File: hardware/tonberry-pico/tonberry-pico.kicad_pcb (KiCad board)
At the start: 2 copper layers, 98 x 53.5 mm, 30 parts, among them J1 MicroSD_Breakout, J2 SparkFun I2S Audio Breakout M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, J3 RC522_Breakout, J4 Adafruit_bq25185_5V, J5 UART, J6 WS2812, J7 Buttons, Q1 2N7000, Q2 2N7000, SW5 SW_Push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

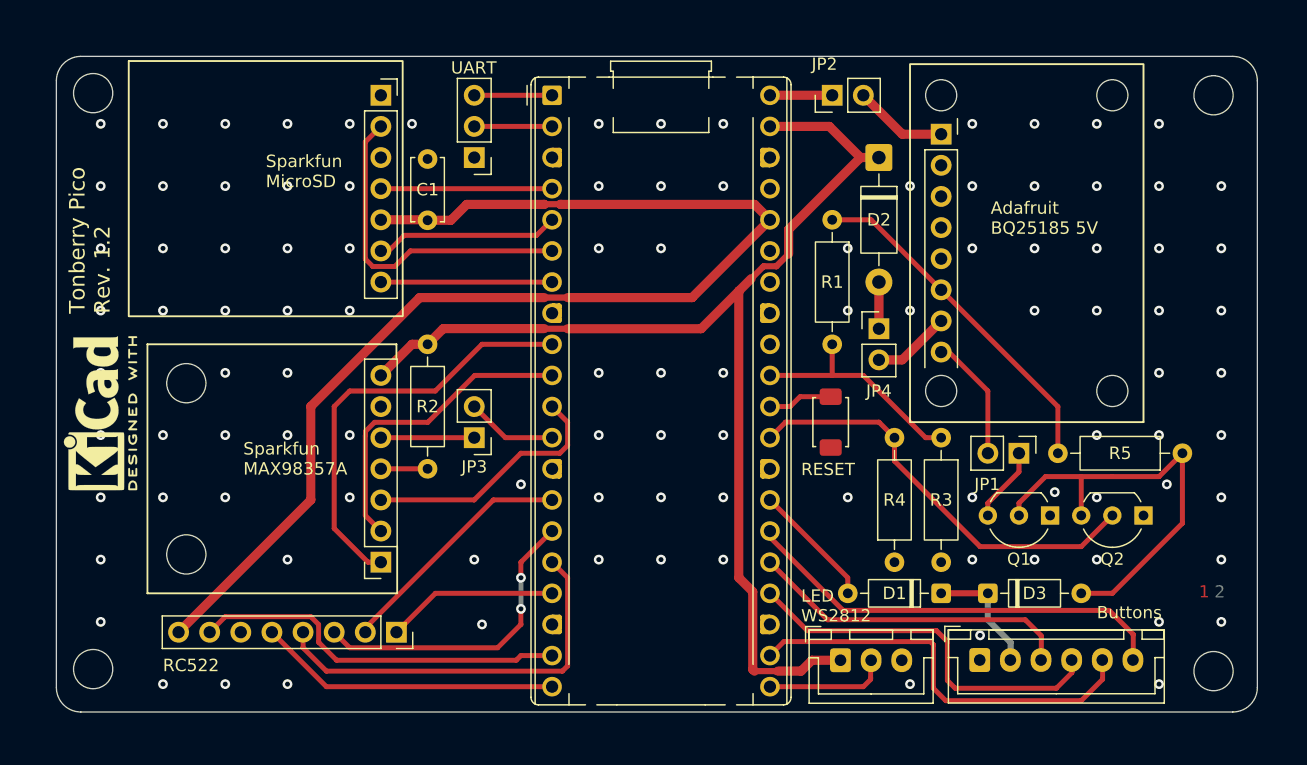
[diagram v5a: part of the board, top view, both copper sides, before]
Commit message: hw: Add GND point for MAX98357 gain config
Add a through-hole pad connected to GND next to the MAX98357 gain config
resistor to allow the user to select from all possible gains.

Signed-off-by: Matthias Blankertz <matthias@blankertz.org>
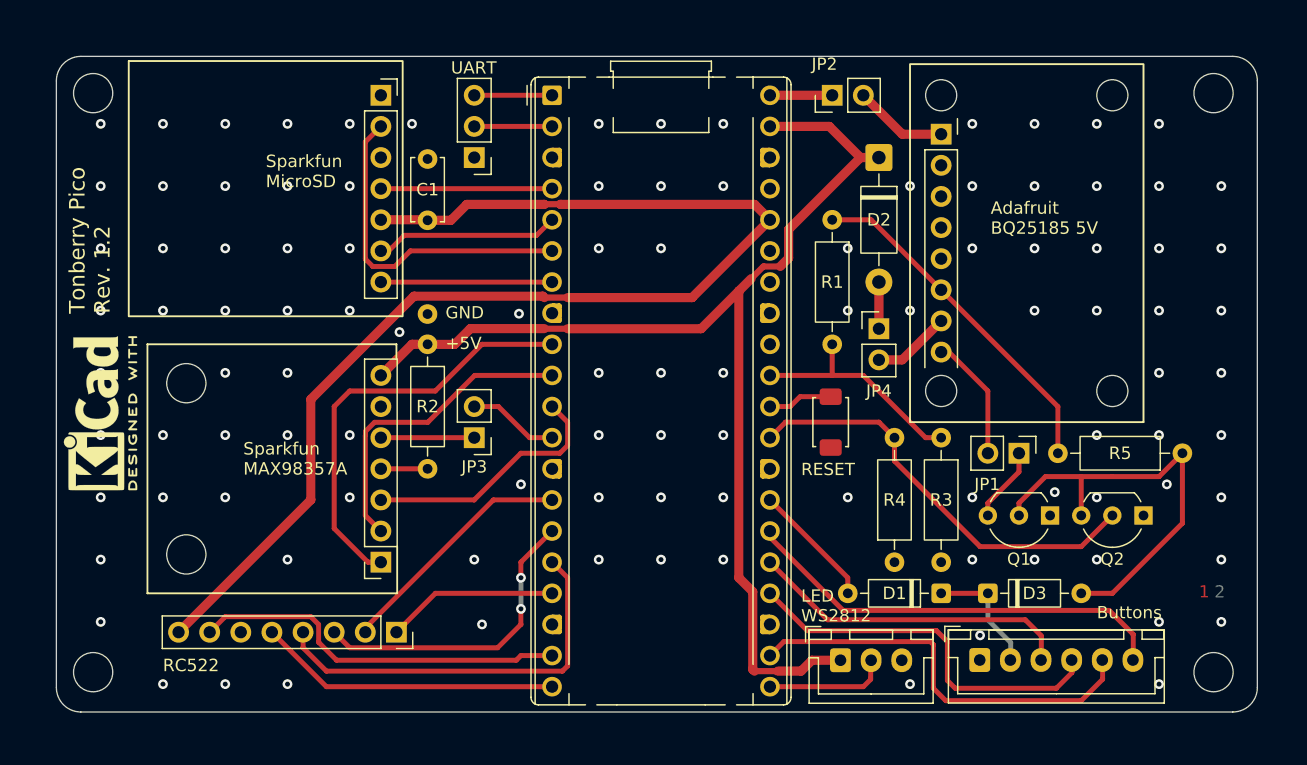
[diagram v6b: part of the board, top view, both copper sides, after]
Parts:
- added J8: Conn_01x01, Connector_Wire:SolderWire-0.25sqmm_1x01_D0.65mm_OD1.7mm, F.Cu at (148.6, 59.1)
- moved REF** 0.25 mm to (121.3, 88.3)
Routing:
- net GND: vias 104 -> 106
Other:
- board text added: "+5V"
- board text added: "GND"
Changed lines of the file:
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@@
 		)
 	)
+	(footprint "Connector_Wire:SolderWire-0.25sqmm_1x01_D0.65mm_OD1.7mm"
+		(layer "F.Cu")
+		(at 148.587019 59.12637)
+		(descr "Soldered wire connection, for a single 0.25 mm² wire, basic insulation, conductor diameter 0.65mm, outer diameter 1.7mm, size source Multi-Contact FLEXI-E_0.25 (https://www.staubli.com/content/dam/ecs/catalogs-brochures/TM/CAB-Main-11014119-en.pdf#page=9), bend radius 3 times outer diameter, generated with kicad-footprint-generator")
+		(tags "connector wire 0.25sqmm")
+		(property "Reference" "J8"
+			(at 0 -2.12 0)
+			(layer "F.SilkS")
+			(hide yes)
+			(effects
+				(font
+					(size 1 1)
+					(thickness 0.15)
+				)
+			)
+		)
+		(property "Value" "Conn_01x01"
+			(at 0 2.12 0)
+			(layer "F.Fab")
+			(effects
+				(font
+					(size 1 1)
+					(thickness 0.15)
+				)
+			)
+		)
+		(property "Datasheet" "~"
+			(at 0 0 0)
+			(layer "F.Fab")
+			(hide yes)
+			(effects
+				(font
+					(size 1.27 1.27)
+					(thickness 0.15)
+				)
+			)
+		)
+		(property "Description" "Generic connector, single row, 01x01, script generated (kicad-library-utils/schlib/autogen/connector/)"
+			(at 0 0 0)
+			(layer "F.Fab")
+			(hide yes)
+			(effects
+				(font
+					(size 1.27 1.27)
+					(thickness 0.15)
+				)
+			)
+		)
+		(property ki_fp_filters "Connector*:*_1x??_*")
+		(sheetname "/")
+		(sheetfile "tonberry-pico.kicad_sch")
+		(attr exclude_from_pos_files)
+		(fp_line
+			(start -1.6 -1.42)
+			(end -1.6 1.42)
+			(stroke
+				(width 0.05)
+				(type solid)
+			)
+			(layer "F.CrtYd")
+		)
+		(fp_line
+			(start -1.6 1.42)
+			(end 1.6 1.42)
+			(stroke
+				(width 0.05)
+				(type solid)
+			)
+			(layer "F.CrtYd")
+		)
+		(fp_line
+			(start 1.6 -1.42)
+			(end -1.6 -1.42)
+			(stroke
+				(width 0.05)
+				(type solid)
+			)
+			(layer "F.CrtYd")
+		)
+		(fp_line
+			(start 1.6 1.42)
+			(end 1.6 -1.42)
+			(stroke
+				(width 0.05)
+				(type solid)
+			)
+			(layer "F.CrtYd")
+		)
+		(fp_circle
+			(center 0 0)
+			(end 0.85 0)
+			(stroke
+				(width 0.1)
+				(type solid)
+			)
+			(fill no)
+			(layer "F.Fab")
+		)
+		(fp_text user "${REFERENCE}"
+			(at 0 0 0)
+			(layer "F.Fab")
+			(effects
+				(font
+					(size 0.42 0.42)
+					(thickness 0.06)
+				)
+			)
+		)
+		(pad "1" thru_hole circle
+			(at 0 0)
+			(size 1.6 1.6)
+			(drill 0.8)
+			(layers "*.Cu" "*.Mask")
+			(remove_unused_layers no)
+			(net 2 "GND")
+			(pinfunction "Pin_1")
+			(pintype "passive")
+		)
+		(embedded_fonts no)
+		(model "${KICAD9_3DMODEL_DIR}/Connector_Wire.3dshapes/SolderWire-0.25sqmm_1x01_D0.65mm_OD1.7mm.step"
+			(offset
+				(xyz 0 0 0)
+			)
+			(scale
+				(xyz 1 1 1)
+			)
+			(rotate
+				(xyz 0 0 0)
+			)
+		)
+	)
 	(footprint "MountingHole:MountingHole_3.2mm_M3_DIN965"
 		(layer "F.Cu")
@@
 		)
 		(pad "" np_thru_hole circle
-			(at 0 0)
+			(at 0 -0.175)
 			(size 3.2 3.2)
 			(drill 3.2)
@@
 		)
 		(pad "" np_thru_hole circle
-			(at 0 0)
+			(at 0 0.085)
 			(size 3.2 3.2)
 			(drill 3.2)
@@
 	(footprint "MountingHole:MountingHole_3.2mm_M3_DIN965"
 		(layer "F.Cu")
-		(at 121.3 88.1)
+		(at 121.3 88.35)
 		(descr "Mounting Hole 3.2mm, M3, no annular, generated by kicad-footprint-generator mountinghole.py")
 		(tags "mountinghole M3 DIN965")
@@
 		(layer "Edge.Cuts")
 	)
+	(gr_text "+5V"
+		(at 150.05 62.1 0)
+		(layer "F.SilkS")
+		(effects
+			(font
+				(size 1 1)
+				(thickness 0.15)
+			)
+			(justify left bottom)
+		)
+	)
 	(gr_text "Sparkfun\nMicroSD"
 		(at 135.382 48.895 0)
@@
 		)
 	)
+	(gr_text "GND"
+		(at 150.05 59.6 0)
+		(layer "F.SilkS")
+		(effects
+			(font
+				(size 1 1)
+				(thickness 0.15)
+			)
+			(justify left bottom)
+		)
+	)
 	(gr_text "LED\nWS2812"
 		(at 179.07 84.328 0)
@@
 	)
 	(segment
+		(start 148.59 61.595)
+		(end 148.595 61.6)
+		(width 0.75)
+		(layer "F.Cu")
+		(net 1)
+	)
+	(segment
 		(start 173.99 80.645)
 		(end 173.99 57.250161)
@@
 	)
 	(segment
-		(start 183.9175 46.355)
-		(end 178.05242 52.22008)
-		(width 0.75)
+		(start 175.99626 55.243902)
+		(end 177.375903 55.243902)
+		(width 0.508)
 		(layer "F.Cu")
 		(net 1)
@@
 	)
 	(segment
-		(start 177.04984 55.23)
-		(end 178.05242 54.22742)
-		(width 0.508)
+		(start 152.085 60.315)
+		(end 158.105002 60.315)
+		(width 0.75)
 		(layer "F.Cu")
 		(net 1)
 	)
 	(segment
-		(start 149.87 60.315)
-		(end 158.105002 60.315)
+		(start 178.05242 54.567385)
+		(end 177.375903 55.243902)
 		(width 0.75)
 		(layer "F.Cu")
@@
 	)
 	(segment
-		(start 176.010162 55.23)
-		(end 177.04984 55.23)
-		(width 0.508)
+		(start 170.915161 60.325)
+		(end 173.99 57.250161)
+		(width 0.75)
 		(layer "F.Cu")
 		(net 1)
 	)
 	(segment
-		(start 170.915161 60.325)
-		(end 173.99 57.250161)
+		(start 148.595 61.6)
+		(end 150.8 61.6)
+		(width 0.75)
+		(layer "F.Cu")
+		(net 1)
+	)
+	(segment
+		(start 178.05242 52.22008)
+		(end 178.05242 54.567385)
 		(width 0.75)
 		(layer "F.Cu")
@@
 	)
 	(segment
-		(start 148.59 61.595)
-		(end 149.87 60.315)
-		(width 0.75)
-		(layer "F.Cu")
-		(net 1)
-	)
-	(segment
 		(start 174.992581 56.247581)
 		(end 173.99 57.250161)
@@
 	)
 	(segment
-		(start 178.05242 52.22008)
-		(end 178.05242 54.22742)
-		(width 0.75)
+		(start 174.992581 56.247581)
+		(end 175.99626 55.243902)
+		(width 0.508)
 		(layer "F.Cu")
 		(net 1)
@@
 	)
 	(segment
-		(start 174.992581 56.247581)
-		(end 176.010162 55.23)
+		(start 160.02 60.325)
+		(end 158.115002 60.325)
 		(width 0.508)
 		(layer "F.Cu")
@@
 	)
 	(segment
-		(start 160.02 60.325)
-		(end 158.115002 60.325)
-		(width 0.508)
+		(start 183.9175 46.355)
+		(end 178.05242 52.22008)
+		(width 0.75)
+		(layer "F.Cu")
+		(net 1)
+	)
+	(segment
+		(start 150.8 61.6)
+		(end 152.085 60.315)
+		(width 0.75)
 		(layer "F.Cu")
 		(net 1)
@@
 	)
 	(via
+		(at 146.3 60.6)
+		(size 0.8)
+		(drill 0.4)
+		(layers "F.Cu" "B.Cu")
+		(free yes)
+		(net 2)
+	)
+	(via
 		(at 172.72 74.085)
 		(size 0.8)
@@
 	)
 	(via
+		(at 156.05 59.1)
+		(size 0.8)
+		(drill 0.4)
+		(layers "F.Cu" "B.Cu")
+		(free yes)
+		(net 2)
+	)
+	(via
 		(at 182.88 74.085)
 		(size 0.8)
@@
 		(start 190.5 81.915)
 		(end 194.31 81.915)
-		(width 0.508)
+		(width 0.4064)
 		(layer "F.Cu")
 		(net 5)
@@
 		(start 196.175 85.939)
 		(end 194.31 84.074)
-		(width 0.508)
+		(width 0.4064)
 		(layer "B.Cu")
 		(net 5)
@@
 		(start 194.31 84.074)
 		(end 194.31 81.915)
-		(width 0.508)
+		(width 0.4064)
 		(layer "B.Cu")
 		(net 5)
@@
 		(start 196.175 86.995)
 		(end 196.175 85.939)
-		(width 0.508)
+		(width 0.4064)
 		(layer "B.Cu")
 		(net 5)
@@
 	)
 	(segment
-		(start 150.495 51.475)
-		(end 151.79 50.18)
+		(start 157.997452 57.66745)
+		(end 158.115002 57.785)
 		(width 0.75)
 		(layer "F.Cu")
@@
 	)
 	(segment
-		(start 139.065 74.295)
-		(end 139.065 66.665)
+		(start 150.495 51.475)
+		(end 151.79 50.18)
 		(width 0.75)
 		(layer "F.Cu")
@@
 	)
 	(segment
-		(start 139.065 66.665)
-		(end 147.945 57.785)
-		(width 0.75)
-		(layer "F.Cu")
-		(net 13)
-	)
-	(segment
 		(start 150.495 51.475)
 		(end 148.59 51.475)
@@
 	)
 	(segment
+		(start 139.065 66.085)
+		(end 147.48255 57.66745)
+		(width 0.75)
+		(layer "F.Cu")
+		(net 13)
+	)
+	(segment
 		(start 158.1 50.18)
 		(end 158.115 50.165)
@@
 	)
 	(segment
-		(start 170.195 57.77)
-		(end 176.53 51.435)
+		(start 139.065 74.295)
+		(end 139.065 66.085)
 		(width 0.75)
 		(layer "F.Cu")
@@
 	)
 	(segment
-		(start 147.945 57.785)
-		(end 158.115002 57.785)
+		(start 170.195 57.77)
+		(end 176.53 51.435)
 		(width 0.75)
 		(layer "F.Cu")
@@
 	)
 	(segment
+		(start 147.48255 57.66745)
+		(end 157.997452 57.66745)
+		(width 0.75)
+		(layer "F.Cu")
+		(net 13)
+	)
+	(segment
 		(start 158.115 50.165)
 		(end 159.425958 50.165)
@@
 	)
 	(segment
+		(start 158.709565 69.174565)
+		(end 158.75 69.215)
+		(width 0.2032)
+		(layer "F.Cu")
+		(net 47)
+	)
+	(segment
 		(start 152.4 66.675)
-		(end 154.94 69.215)
+		(end 154.375 66.675)
 		(width 0.4064)
 		(layer "F.Cu")
@@
 	)
 	(segment
-		(start 158.709565 69.174565)
+		(start 156.915 69.215)
 		(end 158.75 69.215)
-		(width 0.2032)
+		(width 0.4064)
 		(layer "F.Cu")
 		(net 47)
 	)
 	(segment
-		(start 154.94 69.215)
-		(end 158.75 69.215)
+		(start 154.375 66.675)
+		(end 156.915 69.215)
 		(width 0.4064)
 		(layer "F.Cu")

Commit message: hw: Update metadata, move silkscreen board name + rev
No netlist or routing changes.

Signed-off-by: Matthias Blankertz <matthias@blankertz.org>
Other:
- board text added: "Tonberry Pico Rev. ${REVISION} ${ISSUE_DATE}"
- board text removed: "Tonberry Pico Rev. 1.2"
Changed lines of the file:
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@@
 	)
 	(paper "A4")
+	(title_block
+		(title "Tonberry Pico")
+		(date "2025-11-08")
+		(rev "1.2")
+		(comment 1 "Copyright (c) 2025 Matthias Blankertz <matthias@blankertz.org>")
+		(comment 2 "SPDX-License-Identifier: MIT")
+	)
 	(layers
 		(0 "F.Cu" signal)
@@
 	)
 	(footprint "MountingHole:MountingHole_3.2mm_M3_DIN965"
+		(locked yes)
 		(layer "F.Cu")
 		(at 212.725 41.275)
@@
 	)
 	(footprint "MountingHole:MountingHole_3.2mm_M3_DIN965"
+		(locked yes)
 		(layer "F.Cu")
 		(at 212.725 88.265)
@@
 	)
 	(footprint "MountingHole:MountingHole_3.2mm_M3_DIN965"
+		(locked yes)
 		(layer "F.Cu")
 		(at 121.3 41.1)
@@
 	)
 	(footprint "MountingHole:MountingHole_3.2mm_M3_DIN965"
+		(locked yes)
 		(layer "F.Cu")
 		(at 121.3 88.35)
@@
 		)
 	)
-	(gr_text "Tonberry Pico\nRev. 1.2"
-		(at 122.8 59.1 90)
+	(gr_text "Tonberry Pico\nRev. ${REVISION}\n${ISSUE_DATE}"
+		(at 215.55 68.35 90)
 		(layer "F.SilkS")
 		(effects

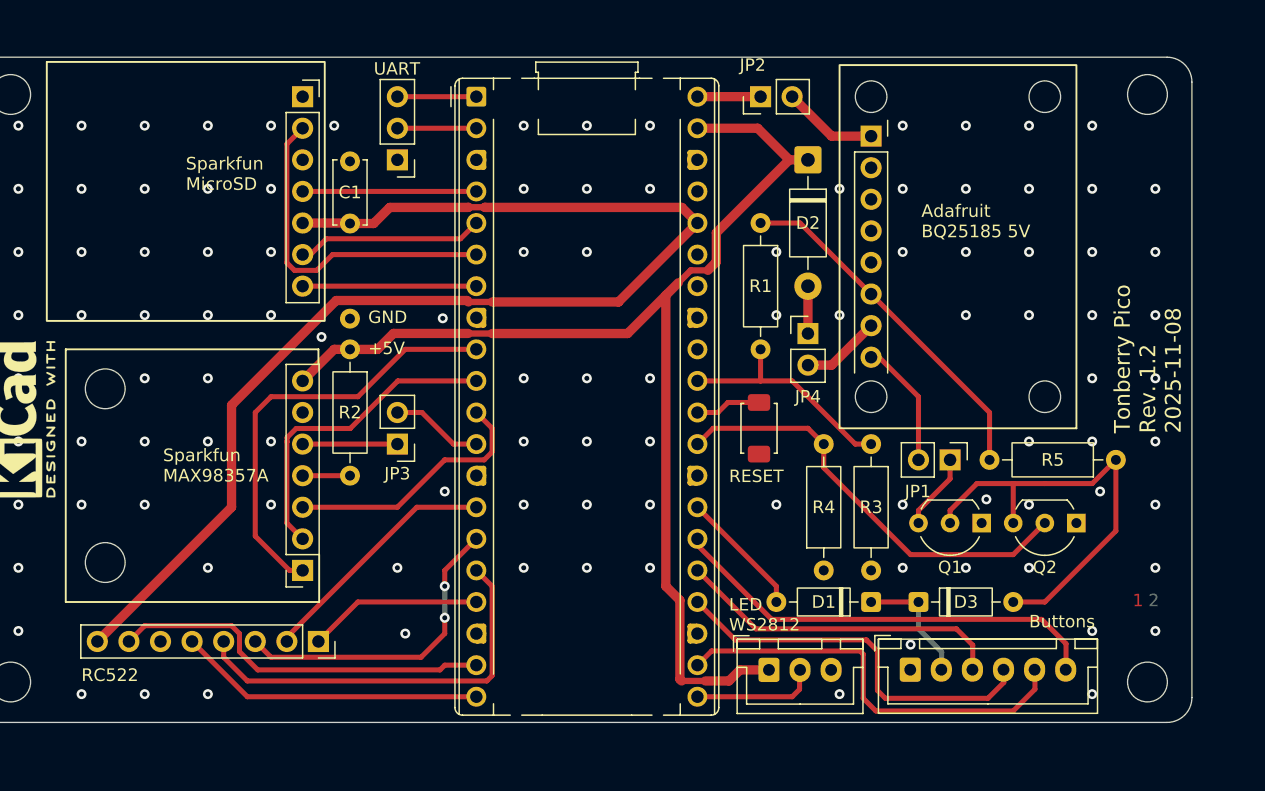
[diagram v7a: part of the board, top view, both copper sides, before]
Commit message: hw: Final fixes for Rev 1.2
- Move RC522 connector a bit further away from the MAX98375 module
  footprint, so a JST-XH connector can be used here too.
- Update custom rules and fix some DRC warnings (no netlist and layout
  changes).

Signed-off-by: Matthias Blankertz <matthias@blankertz.org>
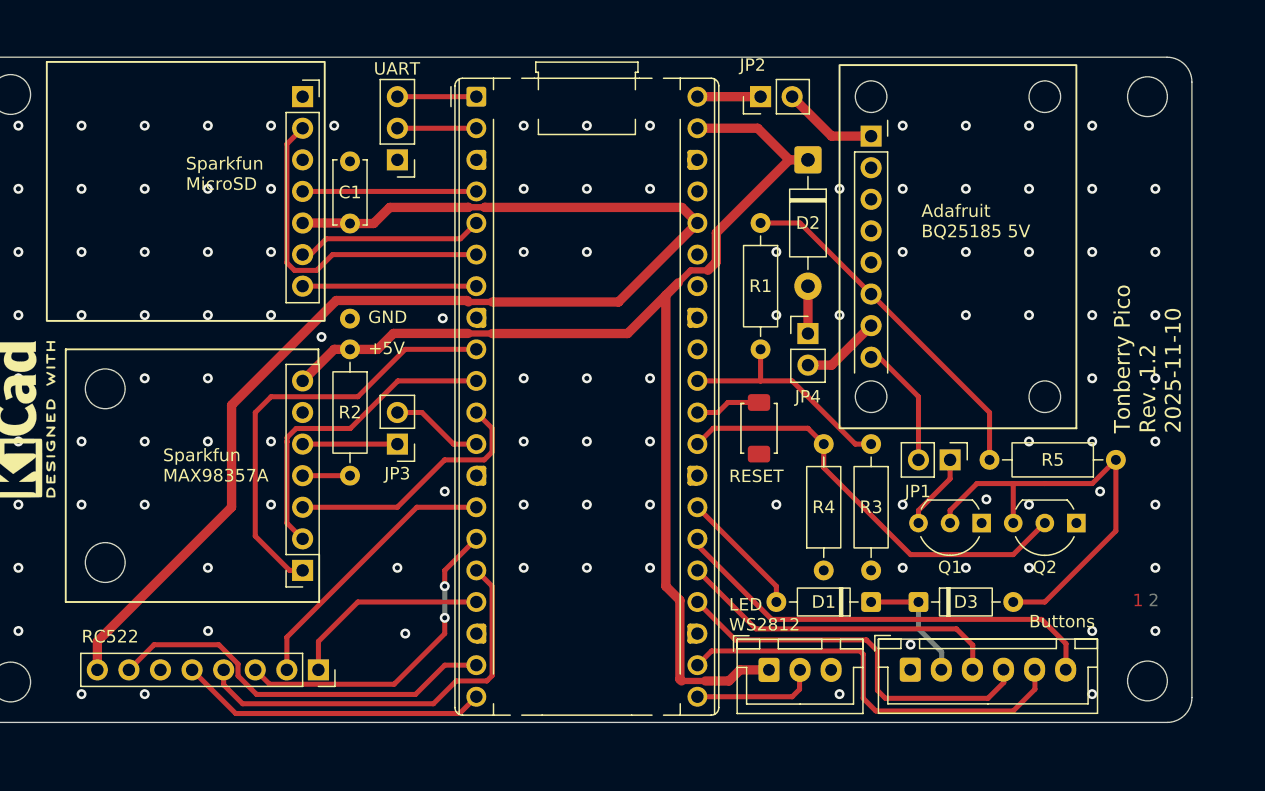
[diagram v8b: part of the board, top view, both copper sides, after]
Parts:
- moved J3 2.28 mm to (146.1, 87.4)
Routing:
- net /RC522_SS: track 14.0 -> 16.3 mm
- net +3V3: track 100.0 -> 102.3 mm
- net /RC522_SCK: track 20.5 -> 22.2 mm
- net /RC522_RST: track 30.9 -> 32.0 mm
- net /RC522_MOSI: track 25.2 -> 26.1 mm
- net /RC522_MISO: track 32.8 -> 33.3 mm
